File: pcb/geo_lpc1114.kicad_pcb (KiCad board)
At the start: 2 copper layers, 100 x 75.7 mm, 133 parts, among them J1 CN_SWD, J10 Screw_Terminal_01x02, J11 Screw_Terminal_01x02, J12 Screw_Terminal_01x02, J13 Screw_Terminal_01x02, J14 Screw_Terminal_01x02, J15 Screw_Terminal_01x02, J16 Screw_Terminal_01x02, J17 Screw_Terminal_01x02, J18 USB_B, J19 MJ-179PH, J2 AQM1602Y-NLW-FBW, J3 GPIO_Header, J4 I2C_Header, J5 UART_Header, J6 Screw_Terminal_01x02, J7 Screw_Terminal_01x02, J8 Screw_Terminal_01x02, J9 Screw_Terminal_01x02, M3 MountingHole_3.2mm_M3, Q3 S8550, Q4 S8550, Q5 S8550, Q6 S8550, Q7 S8550, Q8 S8550, SW1 SW, SW2 SW, U1 LPC1114FN28-102, U10 LPC1114FDH28-102, U11 CH340N, U12 LM2940T-3.3, U4 HX711, U5 HX711, U6 HX711, U7 HX711, U8 HX711, U9 HX711, Y1 12MHz

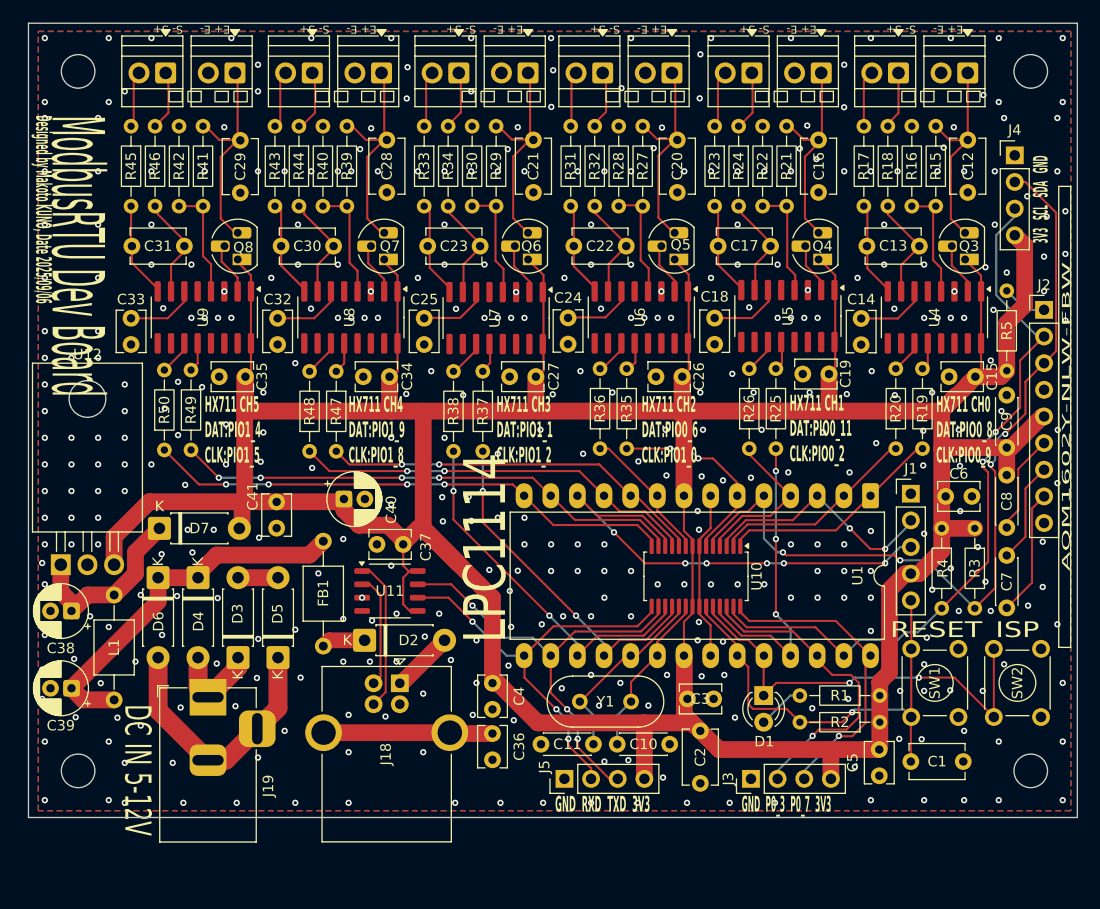
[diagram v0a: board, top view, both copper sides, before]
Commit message: move dir & Fix VDDA/VSSA pin mapping
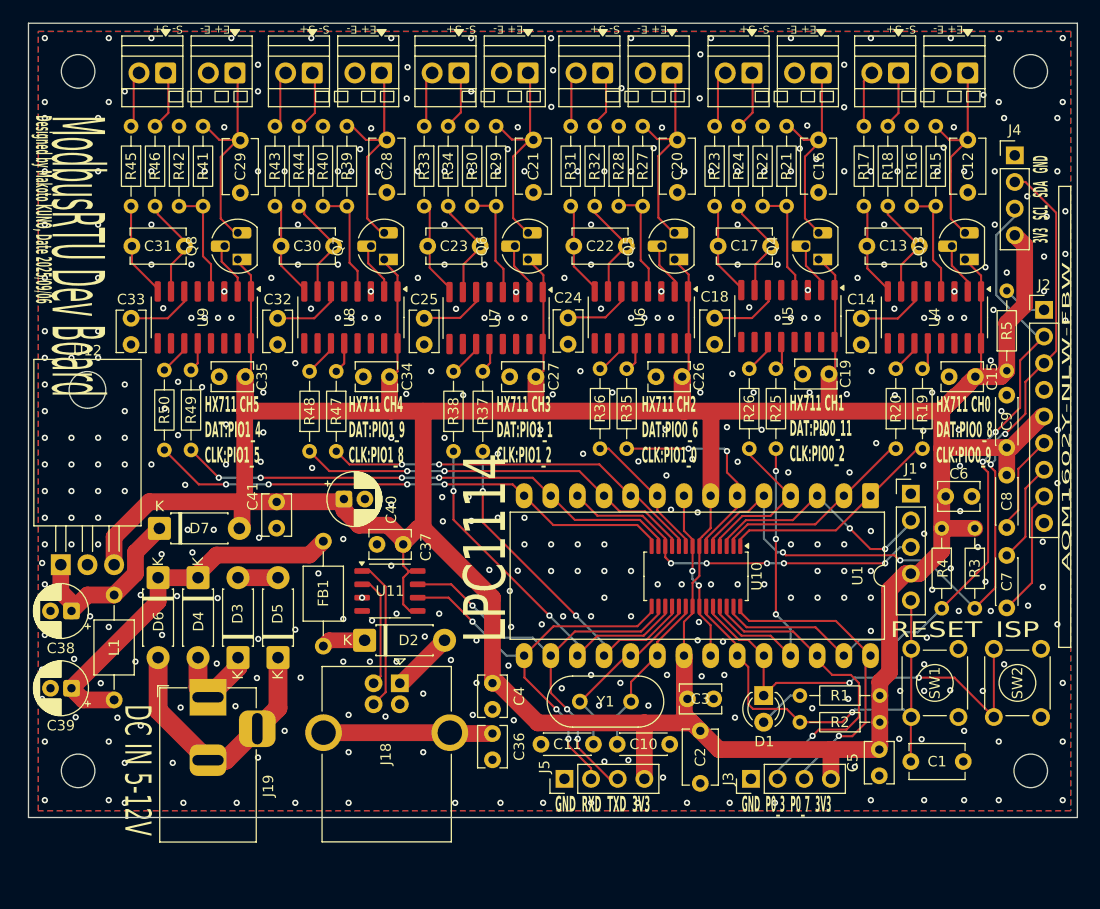
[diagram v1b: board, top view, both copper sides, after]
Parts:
- R1: value 10k -> 4.7k
- U12: footprint Package_TO_SOT_THT:TO-220F-3_Horizontal_TabDown -> Package_TO_SOT_THT:TO-220-3_Horizontal_TabDown
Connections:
- U1 pad 7: GND -> +3V3
- U1 pad 8: +3V3 -> GND
- U10 pad 7: GND -> +3V3
- U10 pad 8: +3V3 -> GND
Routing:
- net SWD_IO: track 46.0 -> 36.2 mm, vias 6 -> 5
- net +3V3: track 408.3 -> 403.9 mm
- net HX711_DAT_2: track 19.2 -> 20.4 mm
- net GND: track 19.9 -> 19.5 mm, vias 396 -> 397

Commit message: AMS1117の裏面サブ実装、基盤の角丸め、ほか微修正
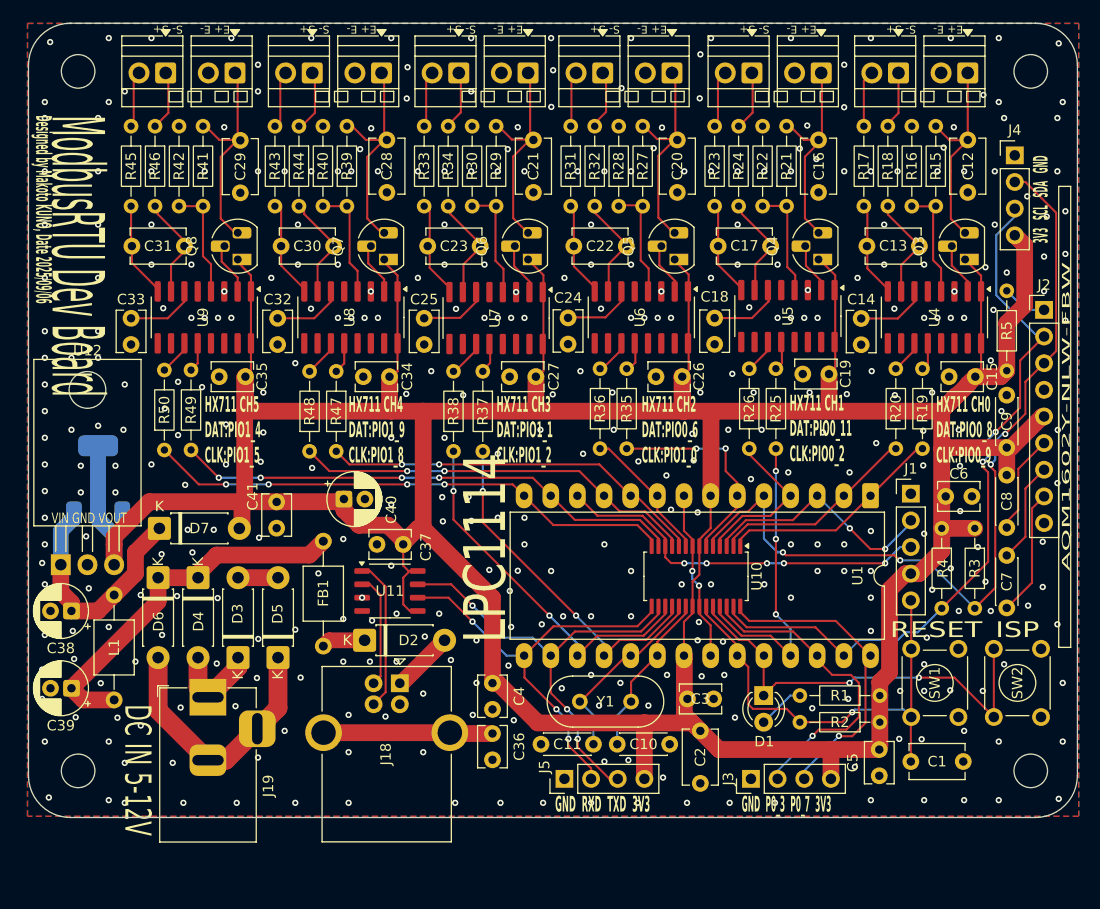
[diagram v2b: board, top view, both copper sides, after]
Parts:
- added U2: AMS1117-3.3, Package_TO_SOT_SMD:SOT-223-3_TabPin2, B.Cu at (86.4, 105.5)
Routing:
- net +3V3: track 403.9 -> 415.8 mm
- net Net-(D7-K): track 17.7 -> 23.2 mm
- net GND: vias 397 -> 384
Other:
- outline, holes or cut-outs redrawn
- board text added: "GND CLK DIO 3V3 RST"
- board text added: "VIN GND VOUT"
